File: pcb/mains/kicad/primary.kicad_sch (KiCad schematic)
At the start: 8 parts, among them J1 43160-0102, J2 43160-0103, J3 43160-0104, J4 43160-0106, K1 G5RL-1A-TV8 DC5, U1 IRM-45-12

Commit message: Prepare compact three-board designs for owner routing
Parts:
- J1: value 43160-0102 -> 43160-1102; MPN 43160-0102 -> 43160-1102
- J2: value 43160-0103 -> 43160-1103; MPN 43160-0103 -> 43160-1103
- J3: value 43160-0104 -> 43160-1104; MPN 43160-0104 -> 43160-1104
- J4: value 43160-0106 -> 43160-1106; MPN 43160-0106 -> 43160-1106
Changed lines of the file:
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@@
 			)
 		)
-		(property "Value" "43160-0103"
+		(property "Value" "43160-1103"
 			(at 114.046 422.54 0)
 			(show_name no)
@@
 			)
 		)
-		(property "MPN" "43160-0103"
-			(at 152.4 398.78 0)
+		(property "MPN" "43160-1103"
+			(at 0 0 0)
 			(hide yes)
 			(show_name no)
@@
 			)
 		)
-		(property "Value" "43160-0106"
+		(property "Value" "43160-1106"
 			(at 684.1359 437.54 0)
 			(show_name no)
@@
 			)
 		)
-		(property "MPN" "43160-0106"
-			(at 721.36 398.78 0)
+		(property "MPN" "43160-1106"
+			(at 0 0 0)
 			(hide yes)
 			(show_name no)
@@
 			)
 		)
-		(property "Value" "43160-0102"
+		(property "Value" "43160-1102"
 			(at 114.046 212.7142 0)
 			(show_name no)
@@
 			)
 		)
-		(property "MPN" "43160-0102"
-			(at 152.4 187.96 0)
+		(property "MPN" "43160-1102"
+			(at 0 0 0)
 			(hide yes)
 			(show_name no)
@@
 			)
 		)
-		(property "Value" "43160-0104"
+		(property "Value" "43160-1104"
 			(at 309.5171 430.04 0)
 			(show_name no)
@@
 			)
 		)
-		(property "MPN" "43160-0104"
-			(at 346.71 398.78 0)
-			(hide yes)
-			(show_name no)
+		(property "MPN" "43160-1104"
+			(at 0 0 0)
+			(hide yes)
+			(show_name no)

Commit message: Simplify mains connectors and separate the 5 V service input
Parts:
- J1: value 43160-1102 -> 1868076; MPN 43160-1102 -> 1868076
- J2: value 43160-1103 -> 1868076; symbol CrystalShim_Mains:Mains_J2 -> CrystalShim_Mains:Mains_J2_Terminal; MPN 43160-1103 -> 1868076
- J3: value 43160-1104 -> 1868076; symbol CrystalShim_Mains:Mains_J3 -> CrystalShim_Mains:Mains_J3_Terminal; MPN 43160-1104 -> 1868076
- J4: value 43160-1106 -> 1868076; symbol CrystalShim_Mains:Mains_J4 -> CrystalShim_Mains:Mains_J4_Terminal; MPN 43160-1106 -> 1868076
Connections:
- no-connect marks 7 -> 0
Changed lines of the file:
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@@
 		)
-	)
-	(no_connect
-		(at 765.81 397.51)
-	)
-	(no_connect
-		(at 765.81 400.05)
-	)
-	(no_connect
-		(at 195.58 398.78)
-	)
-	(no_connect
-		(at 765.81 393.7)
-	)
-	(no_connect
-		(at 389.89 400.05)
-	)
-	(no_connect
-		(at 389.89 397.51)
-	)
-	(no_connect
-		(at 765.81 402.59)
 	)
 	(wire
@@
 	)
 	(symbol
-		(lib_id "CrystalShim_Mains:Mains_J2")
+		(lib_id "CrystalShim_Mains:Mains_J2_Terminal")
 		(at 152.4 398.78 0)
 		(unit 1)
@@
 			)
 		)
-		(property "Value" "43160-1103"
+		(property "Value" "1868076"
 			(at 114.046 422.54 0)
 			(show_name no)
@@
 			)
 		)
-		(property "Datasheet" "https://www.molex.com/content/dam/molex/molex-dot-com/products/automated/en-us/salesdrawingpdf/431/43160/431600106_sd.pdf"
+		(property "Datasheet" "https://www.phoenixcontact.com/en-us/products/pcb-terminal-block-mkds-5-2-762-1868076"
 			(at 152.4 398.78 0)
 			(hide yes)
@@
 			)
 		)
-		(property "MPN" "43160-1103"
+		(property "MPN" "1868076"
 			(at 0 0 0)
 			(hide yes)
@@
 		)
 		(pin "2"
-		)
-		(pin "3"
 		)
 		(instances
@@
 	)
 	(symbol
-		(lib_id "CrystalShim_Mains:Mains_J4")
+		(lib_id "CrystalShim_Mains:Mains_J4_Terminal")
 		(at 721.36 398.78 0)
 		(unit 1)
@@
 			)
 		)
-		(property "Value" "43160-1106"
+		(property "Value" "1868076"
 			(at 684.1359 437.54 0)
 			(show_name no)
@@
 			)
 		)
-		(property "Datasheet" "https://www.molex.com/content/dam/molex/molex-dot-com/products/automated/en-us/salesdrawingpdf/431/43160/431600106_sd.pdf"
+		(property "Datasheet" "https://www.phoenixcontact.com/en-us/products/pcb-terminal-block-mkds-5-2-762-1868076"
 			(at 721.36 398.78 0)
 			(hide yes)
@@
 			)
 		)
-		(property "MPN" "43160-1106"
+		(property "MPN" "1868076"
 			(at 0 0 0)
 			(hide yes)
@@
 		)
 		(pin "2"
-		)
-		(pin "3"
-		)
-		(pin "4"
-		)
-		(pin "5"
-		)
-		(pin "6"
 		)
 		(instances
@@
 			)
 		)
-		(property "Value" "43160-1102"
+		(property "Value" "1868076"
 			(at 114.046 212.7142 0)
 			(show_name no)
@@
 			)
 		)
-		(property "Datasheet" "https://www.molex.com/content/dam/molex/molex-dot-com/products/automated/en-us/salesdrawingpdf/431/43160/431600106_sd.pdf"
+		(property "Datasheet" "https://www.phoenixcontact.com/en-us/products/pcb-terminal-block-mkds-5-2-762-1868076"
 			(at 152.4 187.96 0)
 			(hide yes)
@@
 			)
 		)
-		(property "MPN" "43160-1102"
+		(property "MPN" "1868076"
 			(at 0 0 0)
 			(hide yes)
@@
 	)
 	(symbol
-		(lib_id "CrystalShim_Mains:Mains_J3")
+		(lib_id "CrystalShim_Mains:Mains_J3_Terminal")
 		(at 346.71 398.78 0)
 		(unit 1)
@@
 			)
 		)
-		(property "Value" "43160-1104"
+		(property "Value" "1868076"
 			(at 309.5171 430.04 0)
 			(show_name no)
@@
 			)
 		)
-		(property "Datasheet" "https://www.molex.com/content/dam/molex/molex-dot-com/products/automated/en-us/salesdrawingpdf/431/43160/431600106_sd.pdf"
+		(property "Datasheet" "https://www.phoenixcontact.com/en-us/products/pcb-terminal-block-mkds-5-2-762-1868076"
 			(at 346.71 398.78 0)
 			(hide yes)
@@
 			)
 		)
-		(property "MPN" "43160-1104"
+		(property "MPN" "1868076"
 			(at 0 0 0)
 			(hide yes)
@@
 		(pin "2"
 		)
-		(pin "3"
-		)
-		(pin "4"
-		)
 		(instances

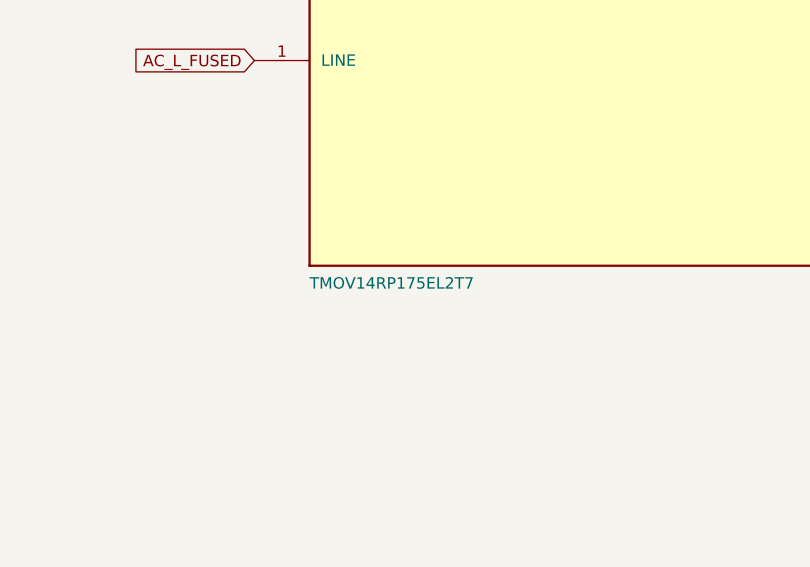
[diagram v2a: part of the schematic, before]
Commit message: Fit the bulk MOV and refresh mains fabrication outputs
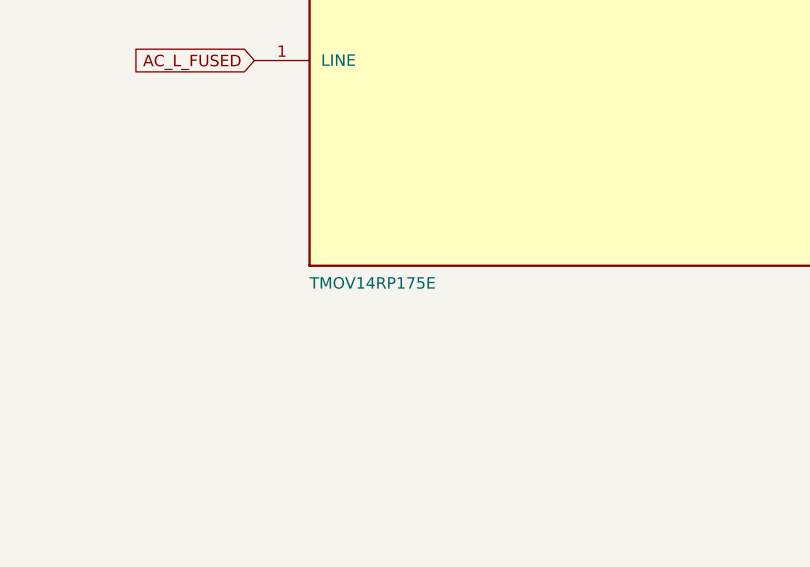
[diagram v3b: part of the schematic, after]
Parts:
- RV1: value TMOV14RP175EL2T7 -> TMOV14RP175E; MPN TMOV14RP175EL2T7 -> TMOV14RP175E
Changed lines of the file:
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@@
 			)
 		)
-		(property "Value" "TMOV14RP175EL2T7"
+		(property "Value" "TMOV14RP175E"
 			(at 263.941 212.7142 0)
 			(show_name no)
@@
 			)
 		)
-		(property "MPN" "TMOV14RP175EL2T7"
+		(property "MPN" "TMOV14RP175E"
 			(at 302.26 187.96 0)
 			(hide yes)
